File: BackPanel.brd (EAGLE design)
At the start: 45 x 18.5 mm, 11 parts

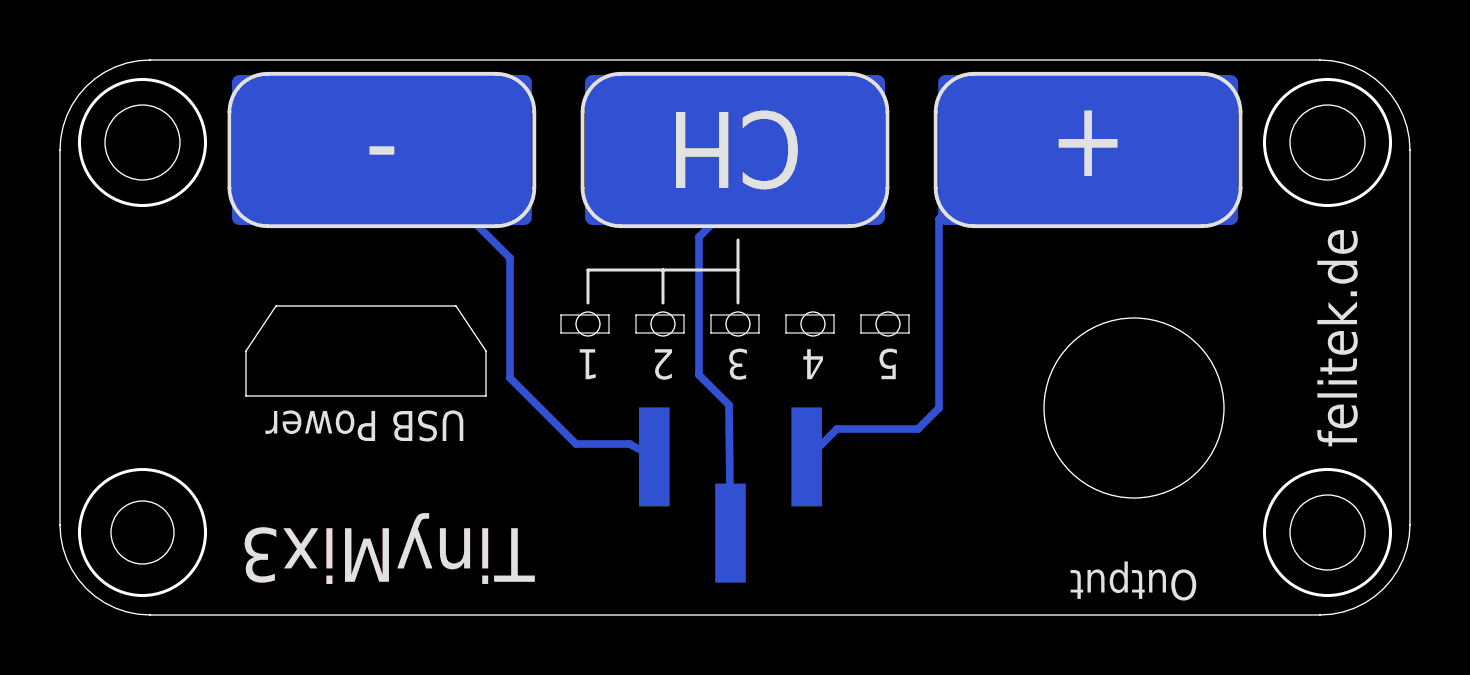
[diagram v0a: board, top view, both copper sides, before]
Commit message: Semi-finalized board, front and back panel Added 100nF capacitor for the TDA7448 mixer
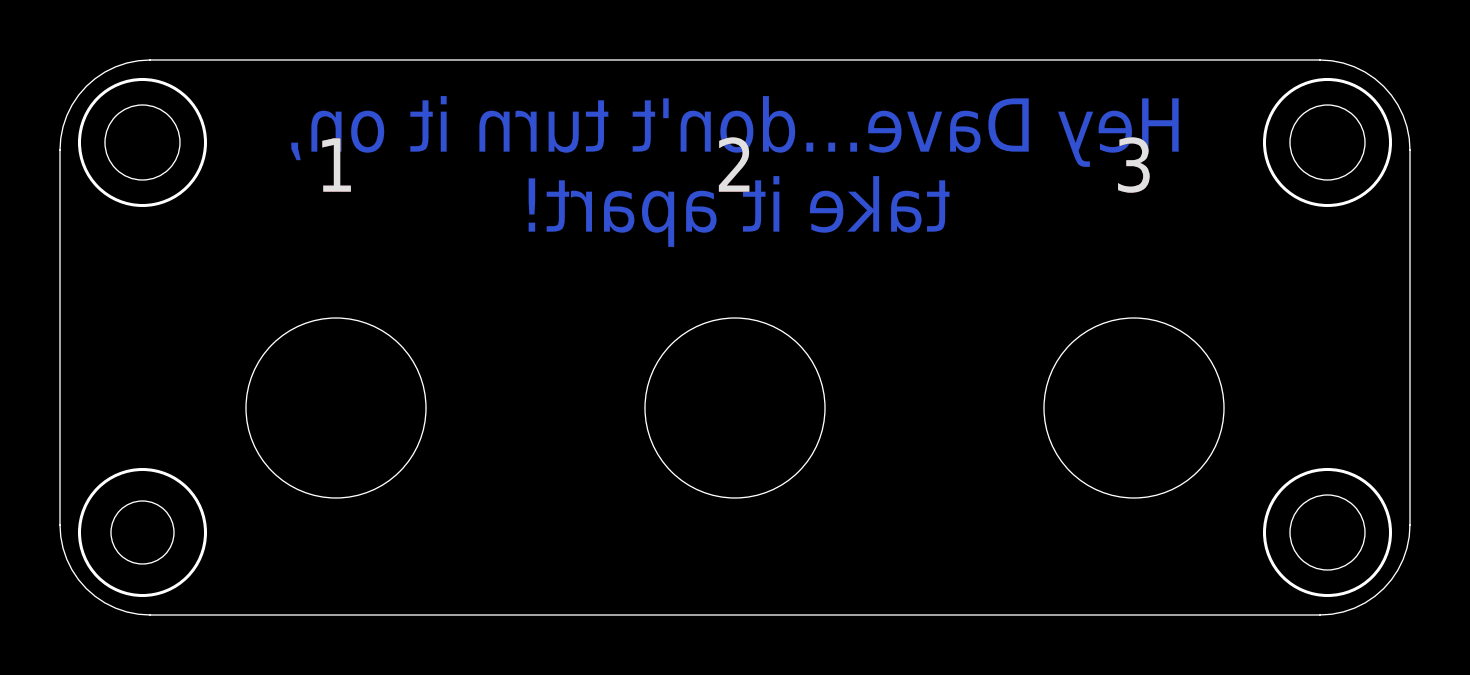
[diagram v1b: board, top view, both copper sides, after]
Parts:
- removed JP1: (no value), pinhead:1X03SMD
- removed U$10, U$8, U$9: TOUCHPAD, TinyMix3-FrontPanel:TOUCH_FIELD_10X5
- removed U$4, U$5, U$6: (no value), TinyMix3-FrontPanel:SMDLED_RIGHTANGLE0602
- removed U$7: (no value), TinyMix3-FrontPanel:SMD-USB-PANEL
- U$2, U$3: device TinyMix3-FrontPanel:SMDLED_RIGHTANGLE0602 -> TinyMix3-FrontPanel:FC68125-FP
- moved U$3 16.0 mm to (9.20, 6.90), turned to 0 degrees
- moved U$2 5.73 mm to (22.5, 6.90), turned to 0 degrees
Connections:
- removed net N$1: JP1.1, U$8.P$1
- removed net N$2: JP1.2, U$9.P$1
- removed net N$3: JP1.3, U$10.P$1
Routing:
- net N$1: track 17.6 -> 0.00 mm
- net N$3: track 15.6 -> 0.00 mm
- net N$2: track 13.7 -> 0.00 mm
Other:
- board text added: "Hey Dave…don't turn it on, take it apart!"
- board text removed: "+"
- board text removed: "-"
- board text removed: "4"
- board text removed: "5"
- board text removed: "CH"
- board text removed: "Output"
- board text removed: "TinyMix3"
- board text removed: "USB Power"
- board text removed: "felitek.de"
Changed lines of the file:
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@@
 <circle x="42.25" y="2.75" radius="2.1" width="0.1" layer="20"/>
 <circle x="42.25" y="15.75" radius="2.1" width="0.1" layer="20"/>
-<text x="22.5" y="15.5" size="2.54" layer="25" rot="SR180" align="center">CH</text>
-<text x="10.73" y="15.8" size="2.54" layer="25" align="center">-</text>
-<text x="34.27" y="15.9" size="2.54" layer="25" align="center">+</text>
-<text x="10.9" y="2" size="1.778" layer="25" rot="SR180" align="center">TinyMix3</text>
-<text x="42.6" y="9.25" size="1.27" layer="25" rot="R270" align="center">felitek.de</text>
-<text x="35.8" y="1" size="1" layer="25" rot="SR180" align="center">Output</text>
-<text x="17.6" y="8.36" size="1" layer="25" rot="SR180" align="center">1</text>
-<text x="20.1" y="8.36" size="1" layer="25" rot="SR180" align="center">2</text>
-<text x="22.6" y="8.36" size="1" layer="25" rot="SR180" align="center">3</text>
-<text x="25.1" y="8.36" size="1" layer="25" rot="SR180" align="center">4</text>
-<text x="27.6" y="8.36" size="1" layer="25" rot="SR180" align="center">5</text>
-<text x="10.2" y="6.3" size="1" layer="25" rot="SR180" align="center">USB Power</text>
-<wire x1="17.6" y1="10.4" x2="17.6" y2="11.5" width="0.1" layer="25"/>
-<wire x1="17.6" y1="11.5" x2="20.1" y2="11.5" width="0.1" layer="25"/>
-<wire x1="20.1" y1="11.5" x2="22.6" y2="11.5" width="0.1" layer="25"/>
-<wire x1="22.6" y1="11.5" x2="22.6" y2="12.5" width="0.1" layer="25"/>
-<wire x1="22.6" y1="11.5" x2="22.6" y2="10.4" width="0.1" layer="25"/>
-<wire x1="20.1" y1="10.4" x2="20.1" y2="11.5" width="0.1" layer="25"/>
-<text x="10.9" y="2" size="1.778" layer="1" rot="SR180" align="center">TinyMix3</text>
+<text x="9.2" y="15" size="1.778" layer="21" align="center">1</text>
+<text x="22.5" y="15" size="1.778" layer="21" align="center">2</text>
+<text x="35.8" y="15" size="1.778" layer="21" align="center">3</text>
+<text x="9.2" y="15" size="1.778" layer="1" align="center">1</text>
+<text x="22.5" y="15" size="1.778" layer="1" align="center">2</text>
+<text x="35.8" y="15" size="1.778" layer="1" align="center">3</text>
+<text x="22.5" y="15" size="1.778" layer="16" rot="MR0" align="center">Hey Dave…don't turn it on,
+take it apart!</text>
 </plain>
 <attributes>
@@
 </autorouter>
 <elements>
-<element name="JP1" library="pinhead" package="1X03SMD" value="" x="22.35" y="4" rot="MR0">
-<attribute name="PRICE_100" value="0.536" x="22.35" y="4" size="1.778" layer="28" rot="MR0" display="off"/>
-<attribute name="OC_DIGIKEY" value="S5595-ND" x="22.35" y="4" size="1.778" layer="28" rot="MR0" display="off"/>
-</element>
 <element name="U$1" library="TinyMix3-FrontPanel" package="FC68125-FP" value="" x="35.8" y="6.9"/>
-<element name="U$2" library="TinyMix3-FrontPanel" package="SMDLED_RIGHTANGLE0602" value="" x="27.5" y="9.7" rot="R180"/>
-<element name="U$3" library="TinyMix3-FrontPanel" package="SMDLED_RIGHTANGLE0602" value="" x="25" y="9.7" rot="R180"/>
-<element name="U$4" library="TinyMix3-FrontPanel" package="SMDLED_RIGHTANGLE0602" value="" x="22.5" y="9.7" rot="R180"/>
-<element name="U$5" library="TinyMix3-FrontPanel" package="SMDLED_RIGHTANGLE0602" value="" x="20" y="9.7" rot="R180"/>
-<element name="U$6" library="TinyMix3-FrontPanel" package="SMDLED_RIGHTANGLE0602" value="" x="17.5" y="9.7" rot="R180"/>
-<element name="U$7" library="TinyMix3-FrontPanel" package="SMD-USB-PANEL" value="" x="10.2" y="8.8" rot="R180"/>
-<element name="U$8" library="TinyMix3-FrontPanel" package="TOUCH_FIELD_10X5" value="TOUCHPAD" x="34.27" y="15.5"/>
-<element name="U$9" library="TinyMix3-FrontPanel" package="TOUCH_FIELD_10X5" value="TOUCHPAD" x="22.5" y="15.5"/>
-<element name="U$10" library="TinyMix3-FrontPanel" package="TOUCH_FIELD_10X5" value="TOUCHPAD" x="10.73" y="15.5"/>
+<element name="U$2" library="TinyMix3-FrontPanel" package="FC68125-FP" value="" x="22.5" y="6.9"/>
+<element name="U$3" library="TinyMix3-FrontPanel" package="FC68125-FP" value="" x="9.2" y="6.9"/>
 </elements>
 <signals>
-<signal name="N$1">
-<contactref element="JP1" pad="1"/>
-<contactref element="U$8" pad="P$1"/>
-<wire x1="24.89" y1="5.27" x2="24.84" y2="5.14" width="0.254" layer="16"/>
-<wire x1="24.84" y1="5.14" x2="25.9" y2="6.2" width="0.254" layer="16"/>
-<wire x1="25.9" y1="6.2" x2="28.6" y2="6.2" width="0.254" layer="16"/>
-<wire x1="28.6" y1="6.2" x2="29.3" y2="6.9" width="0.254" layer="16"/>
-<wire x1="29.3" y1="6.9" x2="29.3" y2="13.2" width="0.254" layer="16"/>
-<wire x1="29.3" y1="13.2" x2="31.3" y2="15.2" width="0.254" layer="16"/>
-<wire x1="31.3" y1="15.2" x2="33.97" y2="15.2" width="0.254" layer="16"/>
-<wire x1="33.97" y1="15.2" x2="34.27" y2="15.5" width="0.254" layer="16"/>
-</signal>
-<signal name="N$2">
-<contactref element="JP1" pad="2"/>
-<contactref element="U$9" pad="P$1"/>
-<wire x1="22.35" y1="2.73" x2="22.3" y2="7" width="0.254" layer="16"/>
-<wire x1="22.3" y1="7" x2="21.3" y2="8" width="0.254" layer="16"/>
-<wire x1="21.3" y1="8" x2="21.3" y2="12.6" width="0.254" layer="16"/>
-<wire x1="21.3" y1="12.6" x2="22.5" y2="13.8" width="0.254" layer="16"/>
-<wire x1="22.5" y1="13.8" x2="22.5" y2="15.5" width="0.254" layer="16"/>
-</signal>
-<signal name="N$3">
-<contactref element="JP1" pad="3"/>
-<contactref element="U$10" pad="P$1"/>
-<wire x1="10.73" y1="15.5" x2="11.4" y2="15.5" width="0.254" layer="16"/>
-<wire x1="11.4" y1="15.5" x2="15" y2="11.9" width="0.254" layer="16"/>
-<wire x1="15" y1="11.9" x2="15" y2="7.9" width="0.254" layer="16"/>
-<wire x1="15" y1="7.9" x2="17.2" y2="5.7" width="0.254" layer="16"/>
-<wire x1="17.2" y1="5.7" x2="18.98" y2="5.7" width="0.254" layer="16"/>
-<wire x1="18.98" y1="5.7" x2="19.81" y2="5.27" width="0.254" layer="16"/>
-</signal>
 </signals>
 </board>
 </drawing>
+<compatibility>
+<note version="6.3" minversion="6.2.2" severity="warning">
+Since Version 6.2.2 text objects can contain more than one line,
+which will not be processed correctly with this version.
+</note>
+</compatibility>
 </eagle>
